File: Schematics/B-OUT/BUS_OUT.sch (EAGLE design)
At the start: 38 parts

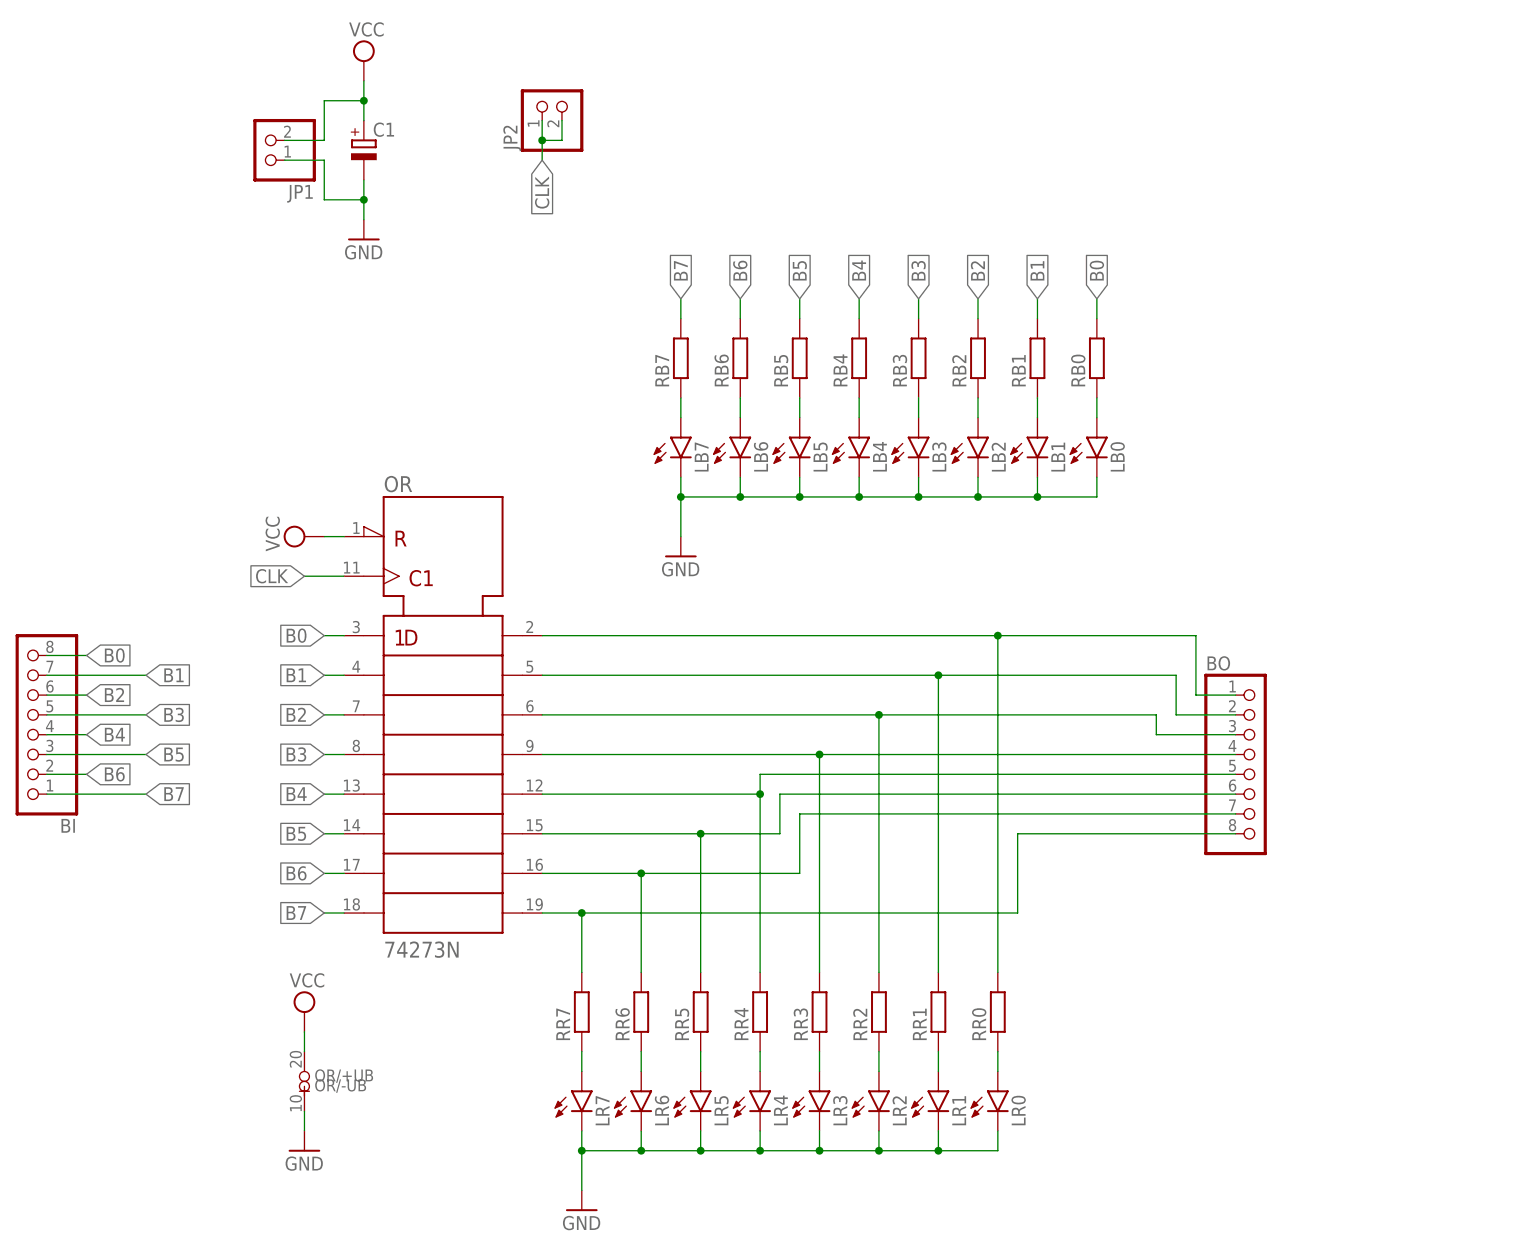
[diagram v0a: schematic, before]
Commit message: Added bus, fixed C1 on ALU-CTRL, CLK.zip, added 7410 to ctrl so bus out will work*.
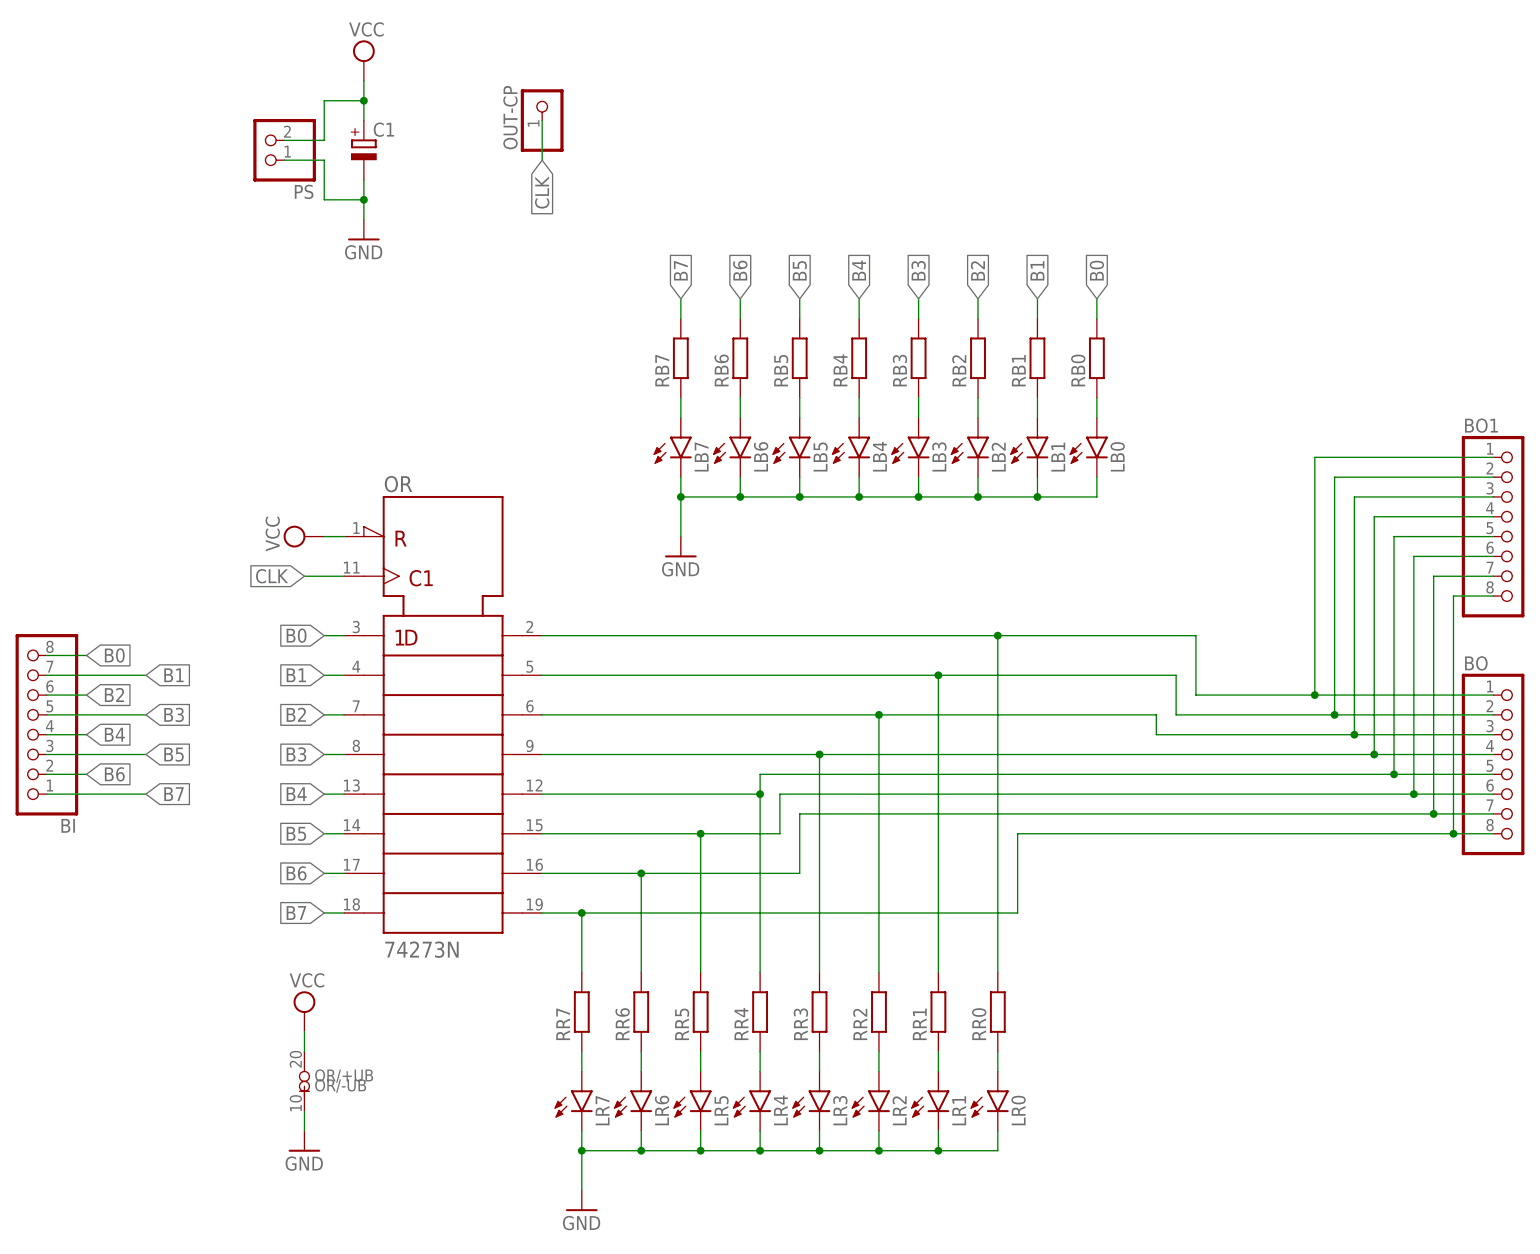
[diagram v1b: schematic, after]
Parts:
- removed JP2: (no value), pinhead:PINHD-1X2
- added BO1: (no value), pinhead:PINHD-1X8
- added OUT-CP: (no value), pinhead:PINHD-1X1
- renumbered JP1 to PS
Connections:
- net CLK: now also OUT-CP.1; no longer JP2.1, JP2.2
- net N$11: now also BO1.8
- net N$14: now also BO1.7
- net N$17: now also BO1.6
- net N$20: now also BO1.5
- net N$23: now also BO1.4
- net N$26: now also BO1.3
- net N$29: now also BO1.2
- net N$32: now also BO1.1
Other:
- moved on the sheet: BO
